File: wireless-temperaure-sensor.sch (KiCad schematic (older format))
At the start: 18 parts, among them J1 Programmer, U1 stm32l010f4, U2 NRF24L01_Breakout, U3 MCP9808_MSOP

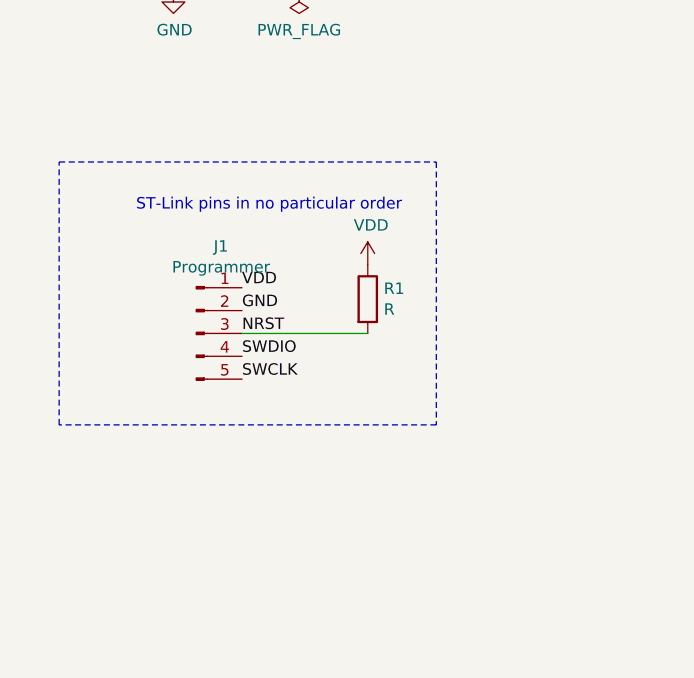
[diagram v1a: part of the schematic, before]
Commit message: Added tact switch to schematic
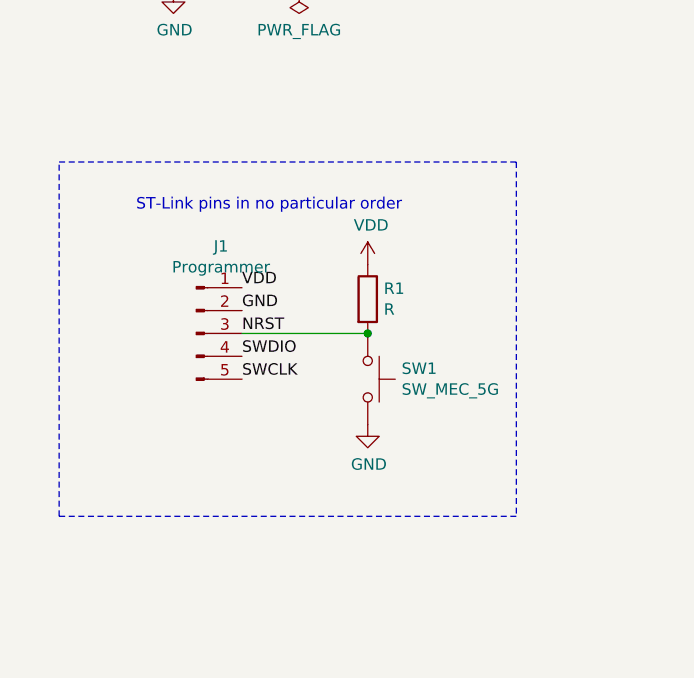
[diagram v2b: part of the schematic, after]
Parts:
- added SW1: SW_MEC_5G, Button_Switch_SMD:SW_Push_SPST_NO_Alps_SKRK, symbol Switch:SW_MEC_5G
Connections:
- net GND: now also SW1.3 (B), SW1.4 (B)
- net NRST: now also SW1.1 (A), SW1.2 (A)
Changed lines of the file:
@@
 ST-Link pins in no particular order\n\n
 Wire Notes Line
-	600  2150 2250 2150
+	600  2150 2600 2150
 Wire Notes Line
-	2250 2150 2250 3300
+	2600 2150 2600 3700
 Wire Notes Line
-	2250 3300 600  3300
+	2600 3700 600  3700
 Wire Notes Line
-	600  3300 600  2150
+	600  3700 600  2150
 Text Label 4250 2850 2    50   ~ 0
 GND
@@
 Text Label 5450 3150 0    50   ~ 0
 SCL
+$Comp
+L Switch:SW_MEC_5G SW1
+U 1 1 5F1B3952
+P 1950 3100
+F 0 "SW1" V 1904 3248 50  0000 L CNN
+F 1 "SW_MEC_5G" V 1995 3248 50  0000 L CNN
+F 2 "Button_Switch_SMD:SW_Push_SPST_NO_Alps_SKRK" H 1950 3300 50  0001 C CNN
+F 3 "http://www.apem.com/int/index.php?controller=attachment&id_attachment=488" H 1950 3300 50  0001 C CNN
+	1    1950 3100
+	0    1    1    0
+$EndComp
+Connection ~ 1950 2900
+$Comp
+L power:GND #PWR0104
+U 1 1 5F1B570B
+P 1950 3300
+F 0 "#PWR0104" H 1950 3050 50  0001 C CNN
+F 1 "GND" H 1955 3127 50  0000 C CNN
+F 2 "" H 1950 3300 50  0001 C CNN
+F 3 "" H 1950 3300 50  0001 C CNN
+	1    1950 3300
+	1    0    0    -1
+$EndComp
 $EndSCHEMATC

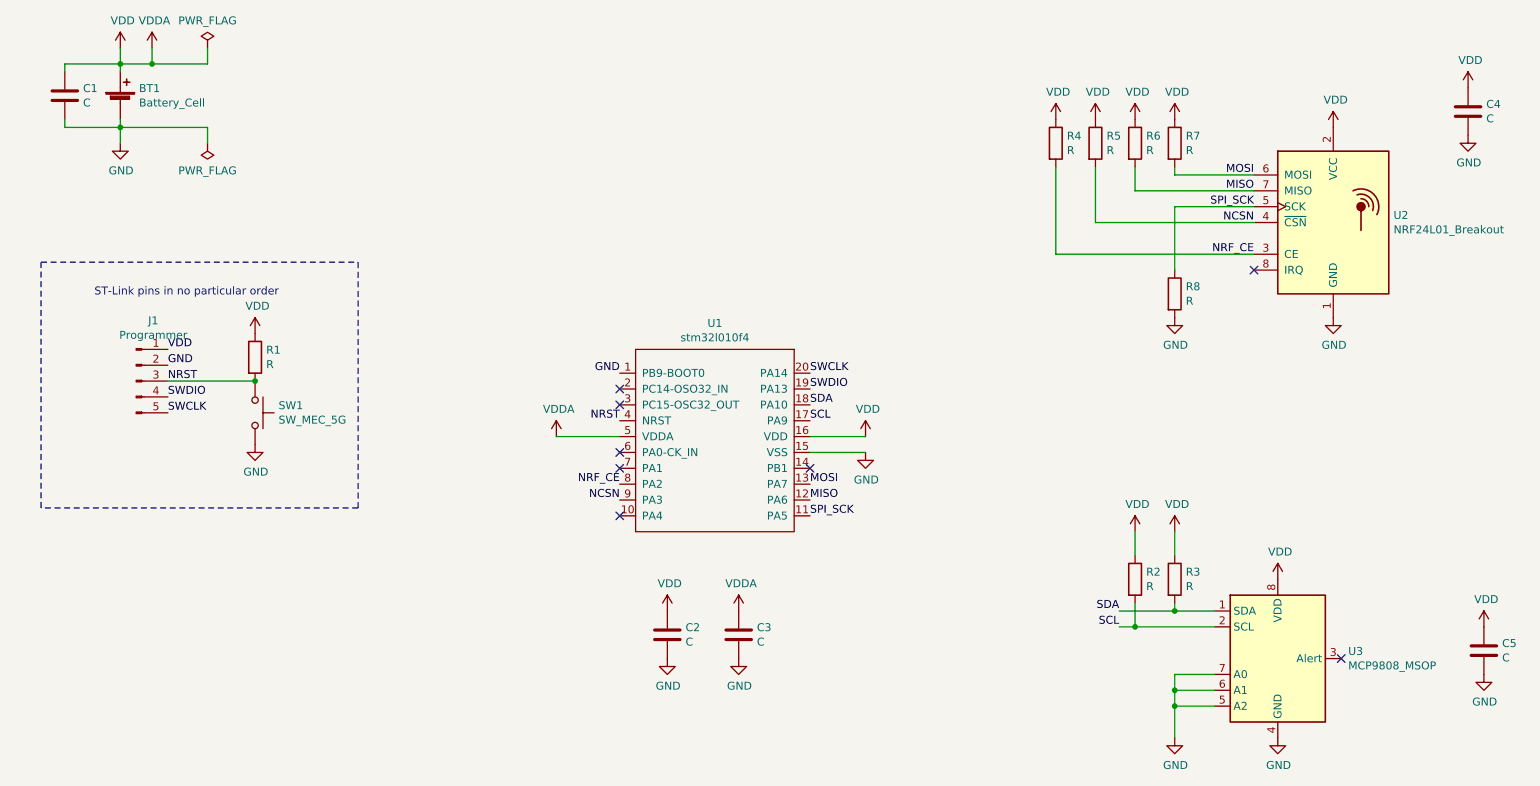
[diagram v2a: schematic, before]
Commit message: Finished schematic and almost finished pcb
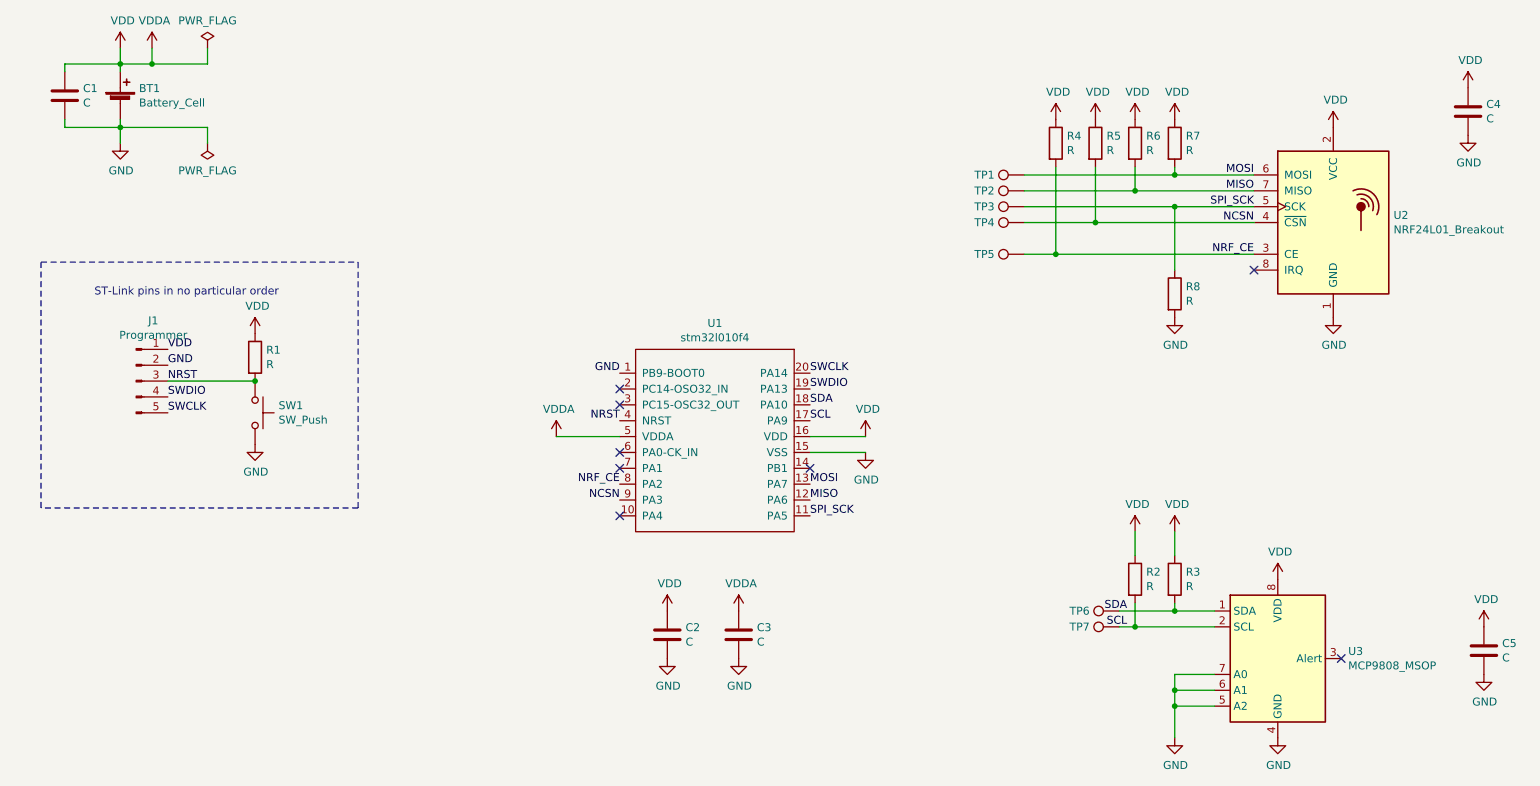
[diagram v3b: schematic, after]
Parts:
- removed SW1: SW_MEC_5G, Button_Switch_SMD:SW_Push_SPST_NO_Alps_SKRK, symbol Switch:SW_MEC_5G
- added SW1: SW_Push, Button_Switch_SMD:SW_Push_SPST_NO_Alps_SKRK, symbol Switch:SW_Push
- added TP1, TP2, TP3, TP4, TP5, TP6, TP7: (no value), TestPoint:TestPoint_THTPad_D1.5mm_Drill0.7mm, symbol Connector:TestPoint
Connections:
- net GND: now also SW1.2
- net MISO: now also TP2.1
- net MOSI: now also TP1.1
- net NCSN: now also TP4.1
- net NRF_CE: now also TP5.1
- net NRST: now also SW1.1
- net SCL: now also TP7.1
- net SDA: now also TP6.1
- net SPI_SCK: now also TP3.1
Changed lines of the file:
@@
 	7500 4450 7400 4450
 Connection ~ 7500 4450
-Text Label 7400 4350 2    50   ~ 0
+Text Label 7450 4350 2    50   ~ 0
 SDA
-Text Label 7400 4450 2    50   ~ 0
+Text Label 7450 4450 2    50   ~ 0
 SCL
 Text Label 5450 3050 0    50   ~ 0
@@
 SCL
 $Comp
-L Switch:SW_MEC_5G SW1
-U 1 1 5F1B3952
-P 1950 3100
-F 0 "SW1" V 1904 3248 50  0000 L CNN
-F 1 "SW_MEC_5G" V 1995 3248 50  0000 L CNN
-F 2 "Button_Switch_SMD:SW_Push_SPST_NO_Alps_SKRK" H 1950 3300 50  0001 C CNN
-F 3 "http://www.apem.com/int/index.php?controller=attachment&id_attachment=488" H 1950 3300 50  0001 C CNN
-	1    1950 3100
-	0    1    1    0
-$EndComp
-Connection ~ 1950 2900
-$Comp
 L power:GND #PWR0104
 U 1 1 5F1B570B
@@
 	1    0    0    -1
 $EndComp
+$Comp
+L Connector:TestPoint TP2
+U 1 1 5F2FAA18
+P 6800 1700
+F 0 "TP2" V 6800 1950 50  0000 C CNN
+F 1 " " V 6904 1772 50  0000 C CNN
+F 2 "TestPoint:TestPoint_THTPad_D1.5mm_Drill0.7mm" H 7000 1700 50  0001 C CNN
+F 3 "~" H 7000 1700 50  0001 C CNN
+	1    6800 1700
+	0    -1   -1   0
+$EndComp
+$Comp
+L Connector:TestPoint TP3
+U 1 1 5F2FAF9D
+P 6800 1800
+F 0 "TP3" V 6800 2050 50  0000 C CNN
+F 1 " " V 6904 1872 50  0000 C CNN
+F 2 "TestPoint:TestPoint_THTPad_D1.5mm_Drill0.7mm" H 7000 1800 50  0001 C CNN
+F 3 "~" H 7000 1800 50  0001 C CNN
+	1    6800 1800
+	0    -1   -1   0
+$EndComp
+$Comp
+L Connector:TestPoint TP4
+U 1 1 5F2FB250
+P 6800 1900
+F 0 "TP4" V 6800 2150 50  0000 C CNN
+F 1 " " V 6904 1972 50  0000 C CNN
+F 2 "TestPoint:TestPoint_THTPad_D1.5mm_Drill0.7mm" H 7000 1900 50  0001 C CNN
+F 3 "~" H 7000 1900 50  0001 C CNN
+	1    6800 1900
+	0    -1   -1   0
+$EndComp
+$Comp
+L Connector:TestPoint TP5
+U 1 1 5F2FBC78
+P 6800 2100
+F 0 "TP5" V 6800 2350 50  0000 C CNN
+F 1 " " V 6904 2172 50  0000 C CNN
+F 2 "TestPoint:TestPoint_THTPad_D1.5mm_Drill0.7mm" H 7000 2100 50  0001 C CNN
+F 3 "~" H 7000 2100 50  0001 C CNN
+	1    6800 2100
+	0    -1   -1   0
+$EndComp
+Wire Wire Line
+	7750 1600 6800 1600
+Connection ~ 7750 1600
+Wire Wire Line
+	7500 1700 6800 1700
+Connection ~ 7500 1700
+Wire Wire Line
+	7750 1800 6800 1800
+Connection ~ 7750 1800
+Wire Wire Line
+	7250 1900 6800 1900
+Connection ~ 7250 1900
+Wire Wire Line
+	7000 2100 6800 2100
+Connection ~ 7000 2100
+$Comp
+L Connector:TestPoint TP6
+U 1 1 5F3066CE
+P 7400 4350
+F 0 "TP6" V 7400 4600 50  0000 C CNN
+F 1 " " V 7504 4422 50  0000 C CNN
+F 2 "TestPoint:TestPoint_THTPad_D1.5mm_Drill0.7mm" H 7600 4350 50  0001 C CNN
+F 3 "~" H 7600 4350 50  0001 C CNN
+	1    7400 4350
+	0    -1   -1   0
+$EndComp
+$Comp
+L Connector:TestPoint TP7
+U 1 1 5F307090
+P 7400 4450
+F 0 "TP7" V 7400 4700 50  0000 C CNN
+F 1 " " V 7504 4522 50  0000 C CNN
+F 2 "TestPoint:TestPoint_THTPad_D1.5mm_Drill0.7mm" H 7600 4450 50  0001 C CNN
+F 3 "~" H 7600 4450 50  0001 C CNN
+	1    7400 4450
+	0    -1   -1   0
+$EndComp
+$Comp
+L Connector:TestPoint TP1
+U 1 1 5F2F9469
+P 6800 1600
+F 0 "TP1" V 6800 1850 50  0000 C CNN
+F 1 " " V 6904 1672 50  0000 C CNN
+F 2 "TestPoint:TestPoint_THTPad_D1.5mm_Drill0.7mm" H 7000 1600 50  0001 C CNN
+F 3 "~" H 7000 1600 50  0001 C CNN
+	1    6800 1600
+	0    -1   -1   0
+$EndComp
+$Comp
+L Switch:SW_Push SW1
+U 1 1 5F36F31F
+P 1950 3100
+F 0 "SW1" V 1904 3248 50  0000 L CNN
+F 1 "SW_Push" V 1995 3248 50  0000 L CNN
+F 2 "Button_Switch_SMD:SW_Push_SPST_NO_Alps_SKRK" H 1950 3300 50  0001 C CNN
+F 3 "~" H 1950 3300 50  0001 C CNN
+	1    1950 3100
+	0    1    1    0
+$EndComp
+Connection ~ 1950 2900
 $EndSCHEMATC
